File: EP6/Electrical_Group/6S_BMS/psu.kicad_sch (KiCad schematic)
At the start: 13 parts, among them Q13 2N7002, Q14 AO3401A, U7 L78L05_SOT89, U8 XC6206PxxxMR

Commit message: [6S_BMS] fixed pcb based on review feedback
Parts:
- C34: footprint Capacitor_SMD:C_0402_1005Metric -> Capacitor_SMD:C_0603_1608Metric
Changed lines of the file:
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@@
 			)
 		)
-		(property "Footprint" "Capacitor_SMD:C_0402_1005Metric"
+		(property "Footprint" "Capacitor_SMD:C_0603_1608Metric"
 			(at 120.65 104.14 0)
 			(effects

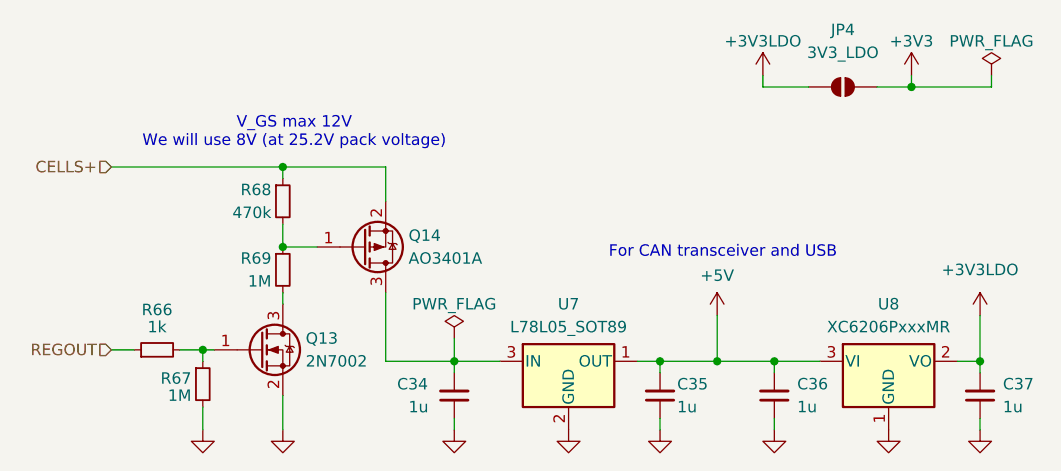
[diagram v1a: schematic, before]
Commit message: batch update for JLCPCB 241117
6SBMS
ACC_HVLV1
INV_CurrentSense2
INV_CurrentSense3
DClinkCap1
INV_MainBoard_STM32
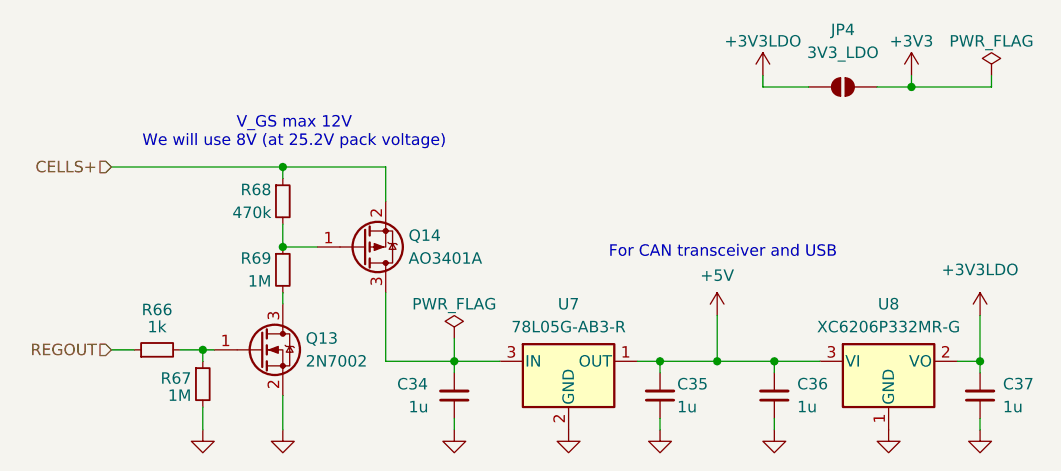
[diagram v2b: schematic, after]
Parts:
- U7: value L78L05_SOT89 -> 78L05G-AB3-R
- U8: value XC6206PxxxMR -> XC6206P332MR-G
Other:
- company: (none) -> NTURacing
- title: (none) -> 6S_BMS
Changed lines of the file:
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@@
 	(generator_version "8.0")
 	(paper "A4")
+	(title_block
+		(title "6S_BMS")
+		(date "2024-11-17")
+		(rev "1.0")
+		(company "NTURacing")
+		(comment 1 "Jerrymk, Jack Kuo")
+	)
 	(junction
 		(at 149.86 100.33)
@@
 			)
 		)
-		(property "Value" "XC6206PxxxMR"
+		(property "Value" "XC6206P332MR-G"
 			(at 168.91 96.52 0)
 			(effects
@@
 			)
 		)
-		(property "Value" "L78L05_SOT89"
+		(property "Value" "78L05G-AB3-R"
 			(at 133.35 96.52 0)
 			(effects

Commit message: [6S_BMS] version 2
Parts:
- removed JP4: 3V3_LDO, Jumper:SolderJumper-2_P1.3mm_Open_TrianglePad1.0x1.5mm, symbol Jumper:SolderJumper_2_Open
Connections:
- net +3V3LDO is gone; now on net +3V3: C37.2, U8.2 (VO)
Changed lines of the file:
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@@
 	(wire
 		(pts
-			(xy 154.94 69.85) (xy 160.02 69.85)
+			(xy 154.94 69.85) (xy 171.45 69.85)
 		)
 		(stroke
@@
 		(pts
 			(xy 101.6 87.63) (xy 105.41 87.63)
-		)
-		(stroke
-			(width 0)
-			(type default)
-		)
-	)
-	(wire
-		(pts
-			(xy 167.64 69.85) (xy 171.45 69.85)
 		)
 		(stroke
@@
 					(unit 1)
 				)
-			)
-		)
-	)
-	(symbol
-		(lib_id "Jumper:SolderJumper_2_Open")
-		(at 163.83 69.85 180)
-		(unit 1)
-		(exclude_from_sim yes)
-		(in_bom no)
-		(on_board yes)
-		(dnp no)
-		(property "Reference" "JP4"
-			(at 163.83 63.5 0)
-			(effects
-				(font
-					(size 1.27 1.27)
-				)
-			)
-		)
-		(property "Value" "3V3_LDO"
-			(at 163.83 66.04 0)
-			(effects
-				(font
-					(size 1.27 1.27)
-				)
-			)
-		)
-		(property "Footprint" "Jumper:SolderJumper-2_P1.3mm_Open_TrianglePad1.0x1.5mm"
-			(at 163.83 69.85 0)
-			(effects
-				(font
-					(size 1.27 1.27)
-				)
-				(hide yes)
-			)
-		)
-		(property "Datasheet" "~"
-			(at 163.83 69.85 0)
-			(effects
-				(font
-					(size 1.27 1.27)
-				)
-				(hide yes)
-			)
-		)
-		(property "Description" "Solder Jumper, 2-pole, open"
-			(at 163.83 69.85 0)
-			(effects
-				(font
-					(size 1.27 1.27)
-				)
-				(hide yes)
-			)
-		)
-		(pin "2"
-		)
-		(pin "1"
-		)
-		(instances
-			(project "6S_BMS"
-				(path "/0942010f-46b1-4fe9-9f5e-a3ebd22b3e41/1b67401b-80bc-4213-a9df-31dbbebac05f"
-					(reference "JP4")
-					(unit 1)
-				)
